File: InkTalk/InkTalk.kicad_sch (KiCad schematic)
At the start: 61 parts, among them J1 USB_C_Receptacle_USB2.0_14P, J4 Conn_ARM_SWD_TagConnect_TC2030, U1 Winbond W25Q16JVUXIQ, U2 LM1117, U3 RP2040, U4 SN65HVD1473DGSR, U5 SN65HVD1473DGSR, X1 12MHz

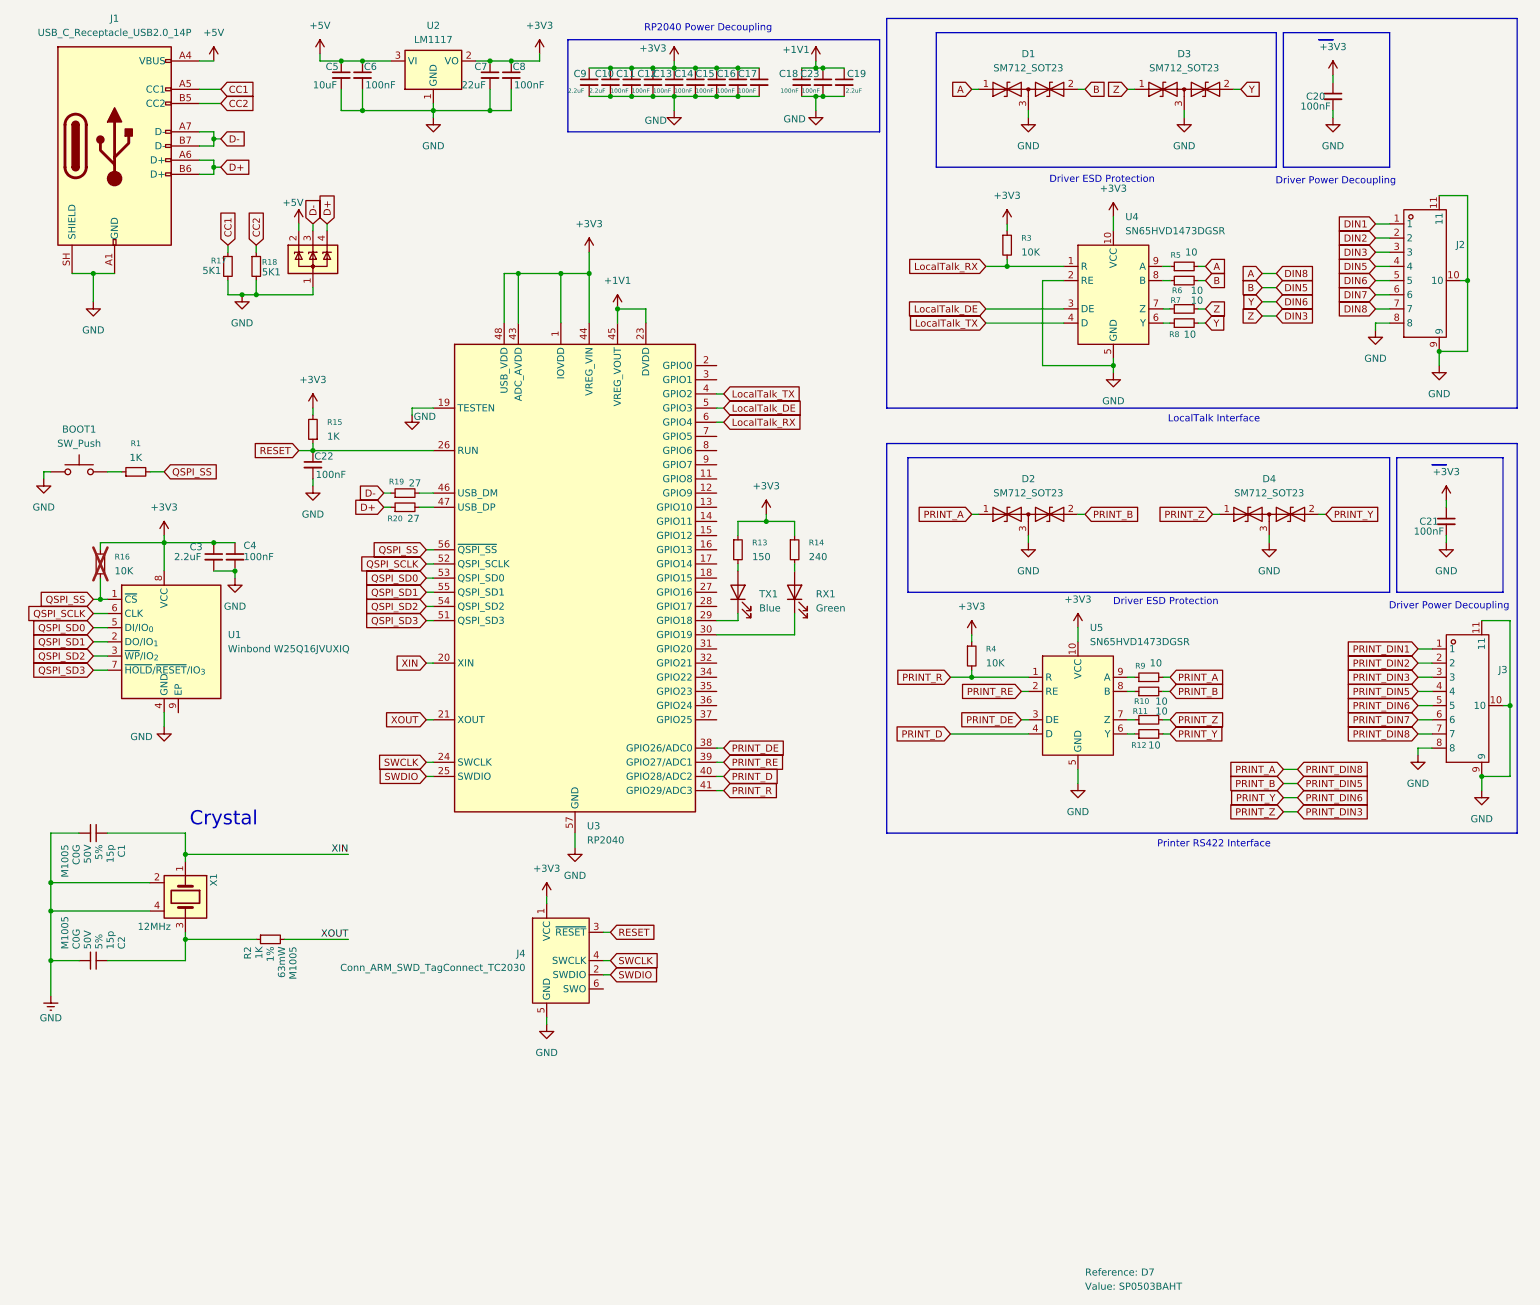
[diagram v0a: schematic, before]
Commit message: InkTalk: Plumb in support for handshake line
I'm unsure if we will _actually_ need this, but this adds in the
option for us to read the handshake status for the printer. One
use for it is getting ThunderScan to work for the ImageWriter which
also uses this line to transfer image data.

Since this is +5v to -5v I've used a little BAT54S diode set with a
big resistor to effectively clamp it to voltage levels safe for the
RP2040. I still need to test this on the prototype units but my napkin
math says it should work.
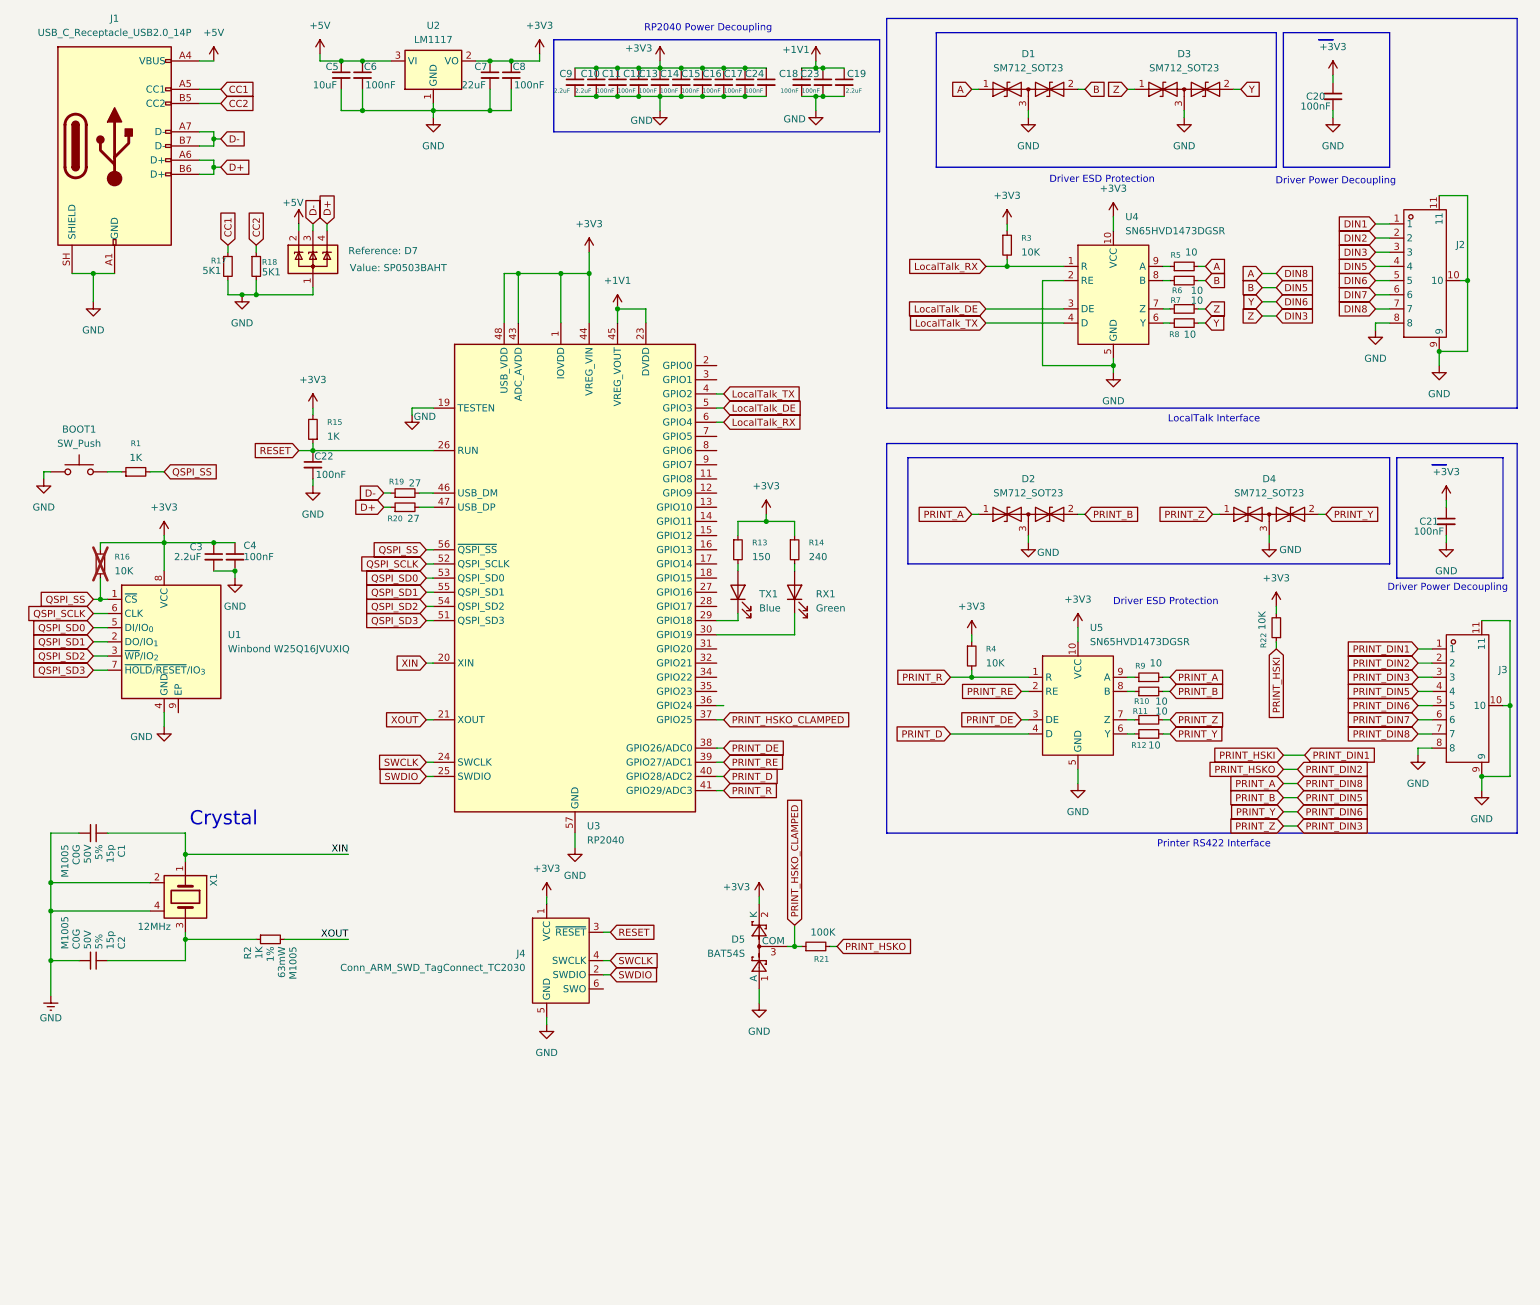
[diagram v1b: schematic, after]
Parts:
- added C24: 100nF, Capacitor_SMD:C_0402_1005Metric, symbol Device:C_Small
- added D5: BAT54S, Package_TO_SOT_SMD:SOT-23, symbol Diode:BAT54S
- added R21: 100K, Resistor_SMD:R_0402_1005Metric, symbol Device:R_Small
- added R22: 10K, Resistor_SMD:R_0402_1005Metric, symbol Device:R_Small
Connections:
- net +3V3: now also C24.1, D5.2 (K), R22.2
- net GND: now also C24.2, D5.1 (A)
- net PRINT_DIN1: now also R22.1
- net PRINT_DIN2: now also R21.2
- net PRINT_HSKO_CLAMPED: now reaches U3.37 (GPIO25)
- net PRINT_HSKO_CLAMPED: now also D5.3 (COM), R21.1
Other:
- moved on the sheet: C10, C11, C12, C13, C14, C15, C16, C17, C9

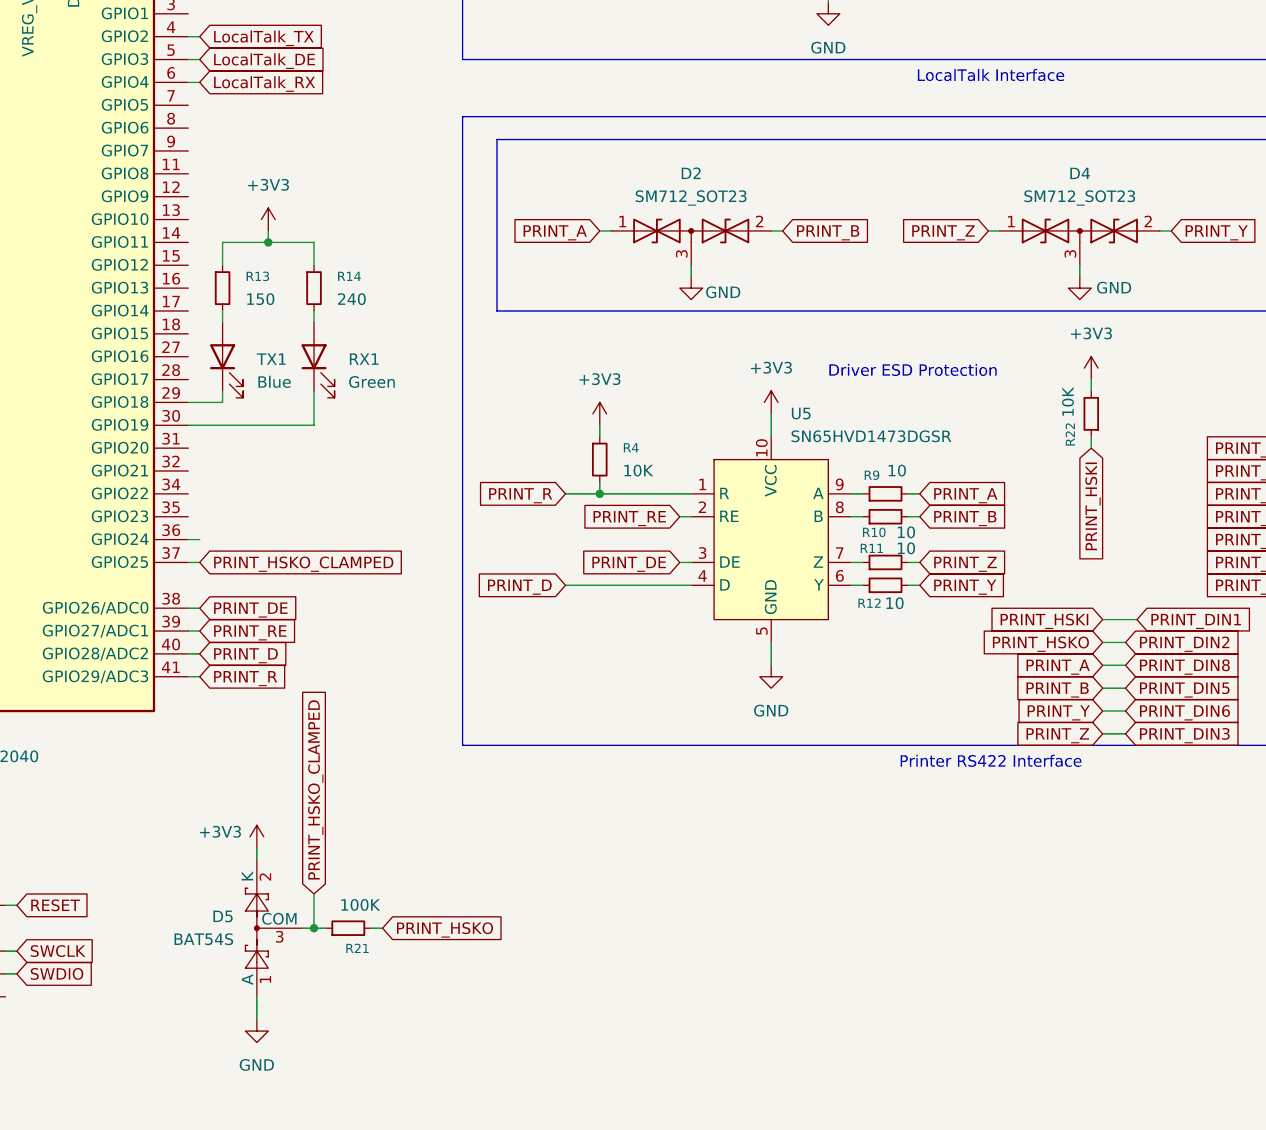
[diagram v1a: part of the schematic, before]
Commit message: InkTalk: Update board design with issues found
InkTalk is _mostly_ functional out of the box, but I found that the
HSKI/HSKO lines were not as optional as I hoped. On StyleWriters the
printer refused to transmit to us unless we actively drove HSKo, and
on ImageWriters the HSKi line must be actively sampled to avoid
overrunning its buffers.

For HSKo we just tie it up to 3.3v with a 10K pull-up. I cant really see
a case where we will receive very large amounts of data from it and would
need to throttle the printer.

For HSKi I've used a simple diode with a pull down resistor so the -5v
signal for "busy" generates a logic 0 for the RP2040, and when actively
driven to +5v we have a basic resistor divider that drops the voltage
enough to be safe within the IOVDD levels. This is then tied to the UART
hardware flow control pin.

These were verified by me manually patching the wires on the board.
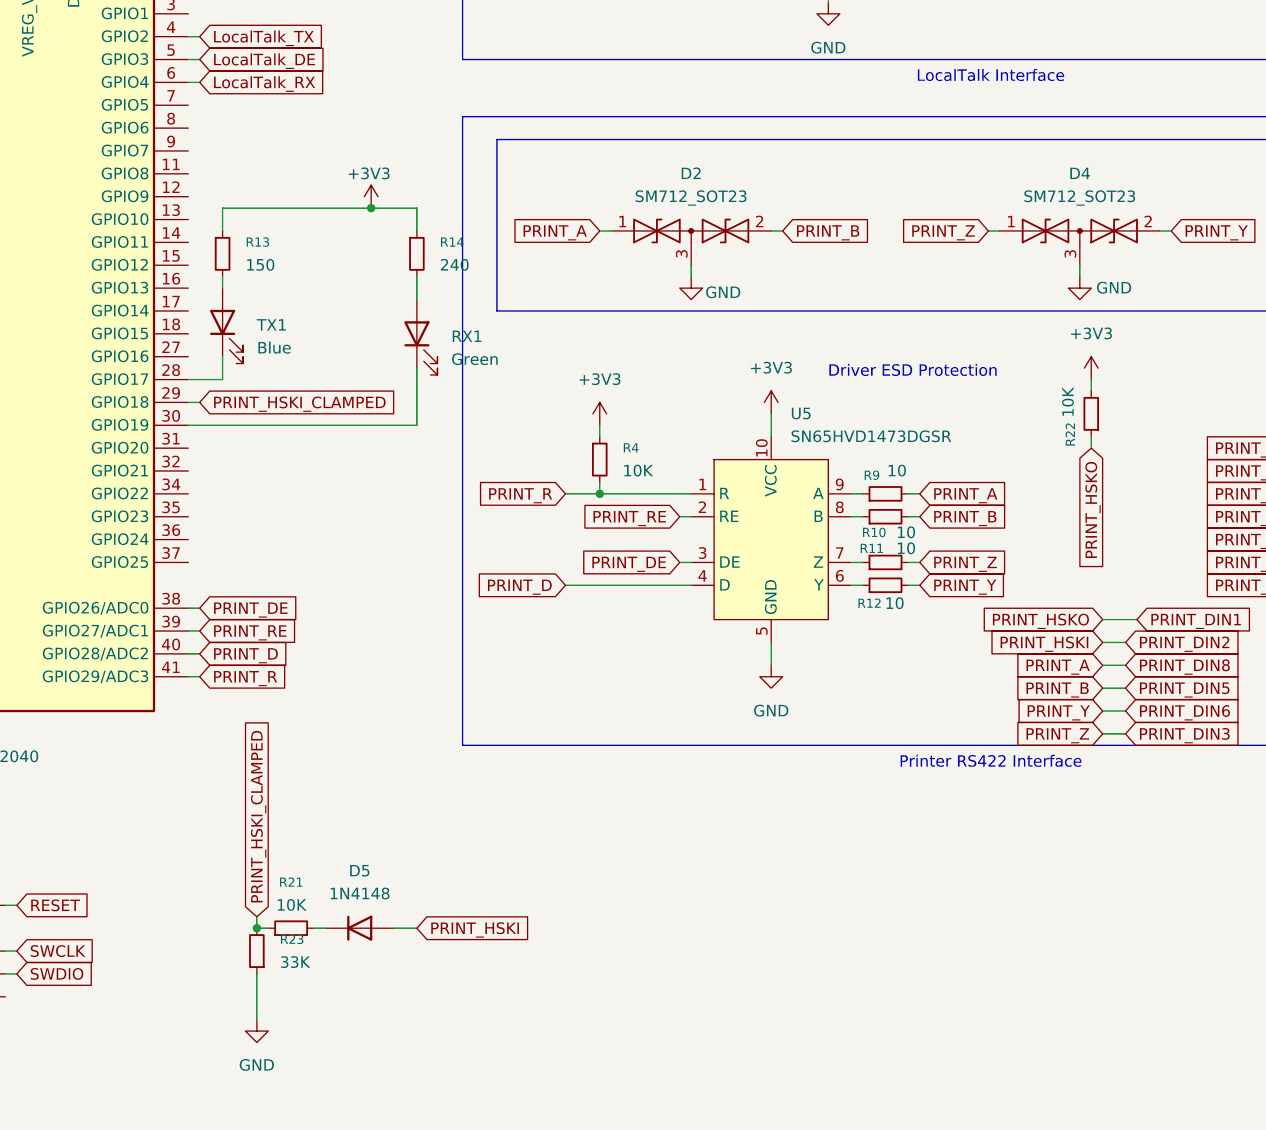
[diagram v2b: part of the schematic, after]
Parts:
- removed D5: BAT54S, Package_TO_SOT_SMD:SOT-23, symbol Diode:BAT54S
- added D5: 1N4148, Diode_SMD:D_SOD-523, symbol Diode:1N4148
- added R23: 33K, Resistor_SMD:R_0402_1005Metric, symbol Device:R_Small
- R21: value 100K -> 10K; LCSC C22859 -> C25804
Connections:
- net GND: now also R23.1
- net PRINT_DIN2: now also D5.2 (A); no longer R21.2
- net at TX1.1 (K): now also U3.28 (GPIO17); no longer U3.29 (GPIO18)
- net PRINT_HSKO_CLAMPED: no longer names the net of U3.37 (GPIO25)
- net PRINT_HSKO_CLAMPED: no longer R21.1
- new net: D5.1 (K), R21.2
- new net PRINT_HSKI_CLAMPED: R21.1, R23.2, U3.29 (GPIO18)
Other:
- moved on the sheet: R13, R14, RX1, TX1
